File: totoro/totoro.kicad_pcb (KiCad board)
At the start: 4 copper layers, 64 x 43 mm, 95 parts, among them J1 USB_B_Micro, J2 SWR201-NRTN-S02-SA-WH, J3 SWR201-NRTN-S02-SA-WH, Q1 MMBT3904, Q2 MMBT3904, Q3 MMBT3904, Q5 2N7002, Q6 MMBT3904, Q7 BC817, Q8 BC817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

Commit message: DRC clean
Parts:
- moved C14 1.28 mm to (156.7, 79.8), turned to 0 degrees
- moved C31 0.67 mm to (157.7, 77.6), turned to 0 degrees
- moved R8 0.38 mm to (151.9, 78.2)
- moved C29 0.36 mm to (141.8, 92.6)
- moved C32 0.11 mm to (155.1, 76.8)
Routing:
- net +3V3: track 39.0 -> 38.2 mm
- net USB_VIN: track 33.5 -> 34.3 mm

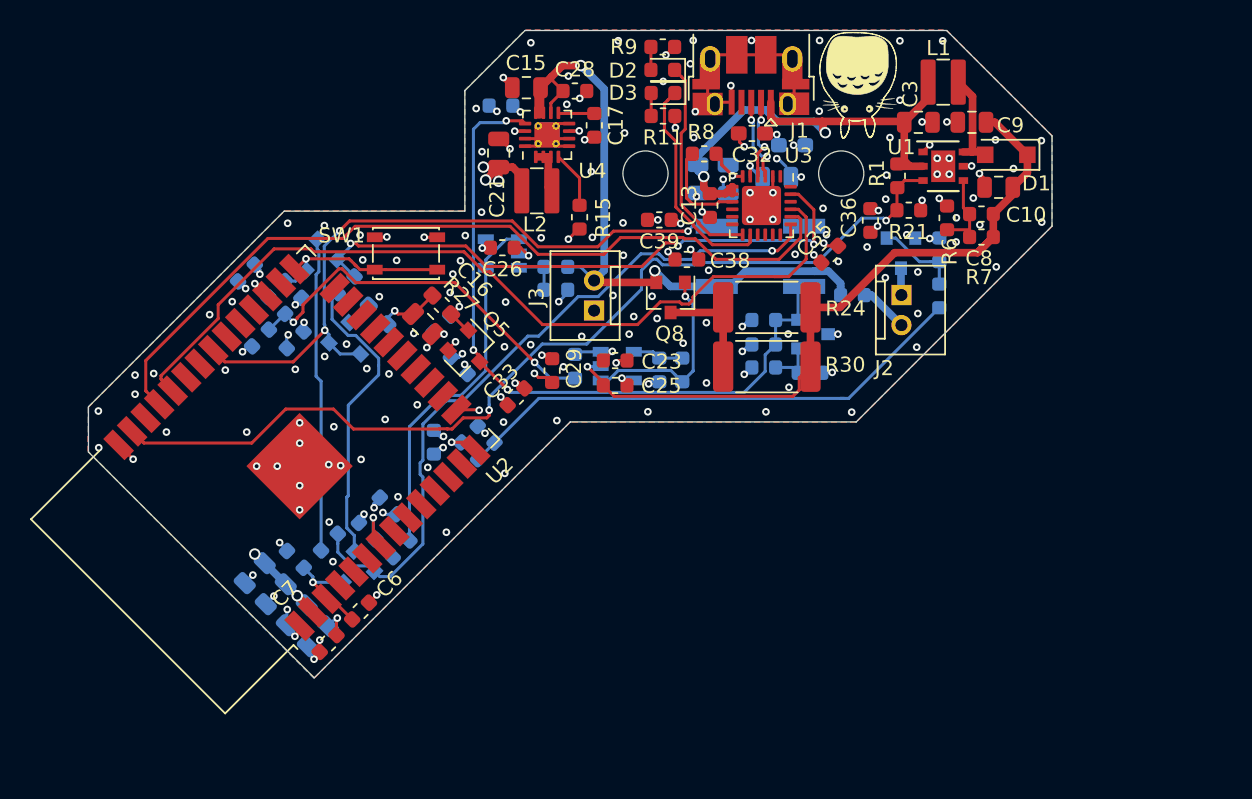
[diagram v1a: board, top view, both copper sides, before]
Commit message: Replaced mounting holes with actual mounting holes
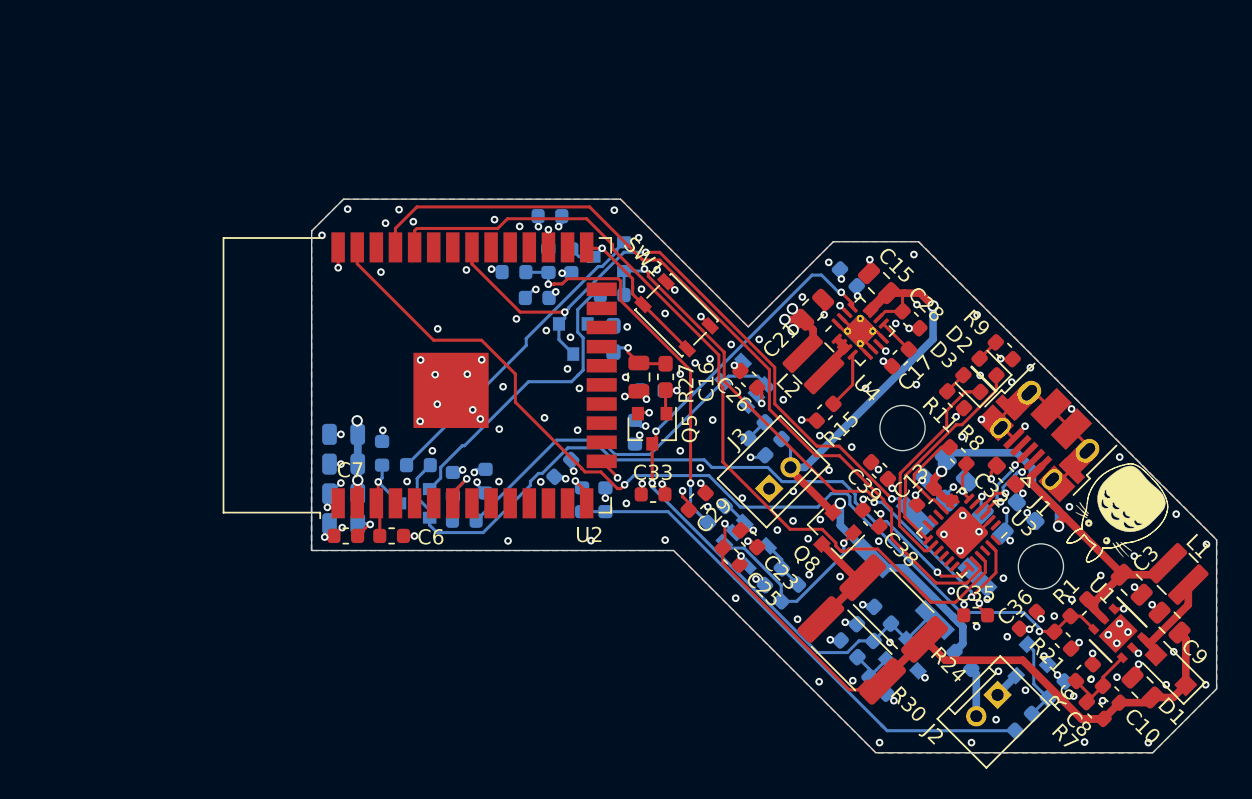
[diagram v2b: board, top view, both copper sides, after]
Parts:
- added REF**: hole, totoro:hole, F.Cu at (174.3, 105.6)
- added REF**: hole, totoro:hole, F.Cu at (165.1, 96.4)
- moved L1 36.2 mm to (183.3, 106.1), turned to 315 degrees
- moved D1 35.9 mm to (182.9, 112.5), turned to 135 degrees
- moved C9 35.7 mm to (182.8, 109.3), turned to 135 degrees
- moved C10 34.6 mm to (181.0, 113.6), turned to 135 degrees
- moved C3 33.8 mm to (180.3, 106.8), turned to 315 degrees
- moved REF** 33.4 mm to (179.3, 102.1), turned to 135 degrees
- moved U1 33.1 mm to (179.4, 110.0), turned to 315 degrees
- moved C8 33.0 mm to (178.9, 114.1), turned to 315 degrees
- moved R7 32.3 mm to (177.9, 115.2), turned to 135 degrees
- moved R6 31.6 mm to (177.2, 112.7), turned to 45 degrees
- moved R1 31.1 mm to (176.8, 108.3), turned to 225 degrees
- moved J1 30.8 mm to (174.6, 96.8), turned to 135 degrees
- moved R9 30.4 mm to (171.8, 91.3), turned to 135 degrees
- moved R21 30.3 mm to (175.7, 110.5), turned to 315 degrees
- moved C22 30.2 mm to (175.3, 113.8), turned to 45 degrees
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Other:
- board size 64 x 43 mm -> 60.1 x 36.8 mm
